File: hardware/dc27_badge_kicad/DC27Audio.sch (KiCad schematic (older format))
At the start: 21 parts, among them U501 CS4344-CZZ, U502 LM4880

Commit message: check in charging circuit changes
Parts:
- removed TP501: DAC_OUT_R, TestPoint:TestPoint_Pad_D2.0mm, symbol Connector:TestPoint
- removed TP502: DAC_OUT_L, TestPoint:TestPoint_Pad_D2.0mm, symbol Connector:TestPoint
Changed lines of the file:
@@
 	4250 3850 4500 3850
+Wire Wire Line
+	4550 4100 4700 4100
 Wire Wire Line
 	4550 3950 4550 4100
@@
 	5000 4100 5300 4100
 Wire Wire Line
-	4250 3650 4600 3650
+	4250 3650 4700 3650
 Wire Wire Line
 	5000 3650 5300 3650
@@
 Text Notes 4850 3350 0    50   ~ 0
 Can drop R502,503 to 15k, \nbut some distortion present.
-$Comp
-L Connector:TestPoint TP501
-U 1 1 5CE34BE7
-P 4600 3050
-F 0 "TP501" H 4658 3168 50  0000 L CNN
-F 1 "DAC_OUT_R" H 4658 3077 50  0000 L CNN
-F 2 "TestPoint:TestPoint_Pad_D2.0mm" H 4800 3050 50  0001 C CNN
-F 3 "~" H 4800 3050 50  0001 C CNN
-	1    4600 3050
-	1    0    0    -1
-$EndComp
-$Comp
-L Connector:TestPoint TP502
-U 1 1 5CE35CF0
-P 4600 4750
-F 0 "TP502" H 4542 4776 50  0000 R CNN
-F 1 "DAC_OUT_L" H 4542 4867 50  0000 R CNN
-F 2 "TestPoint:TestPoint_Pad_D2.0mm" H 4800 4750 50  0001 C CNN
-F 3 "~" H 4800 4750 50  0001 C CNN
-	1    4600 4750
-	-1   0    0    1
-$EndComp
-Wire Wire Line
-	4600 4750 4600 4100
-Wire Wire Line
-	4550 4100 4600 4100
-Connection ~ 4600 4100
-Wire Wire Line
-	4600 4100 4700 4100
-Wire Wire Line
-	4600 3050 4600 3650
-Connection ~ 4600 3650
-Wire Wire Line
-	4600 3650 4700 3650
 $EndSCHEMATC

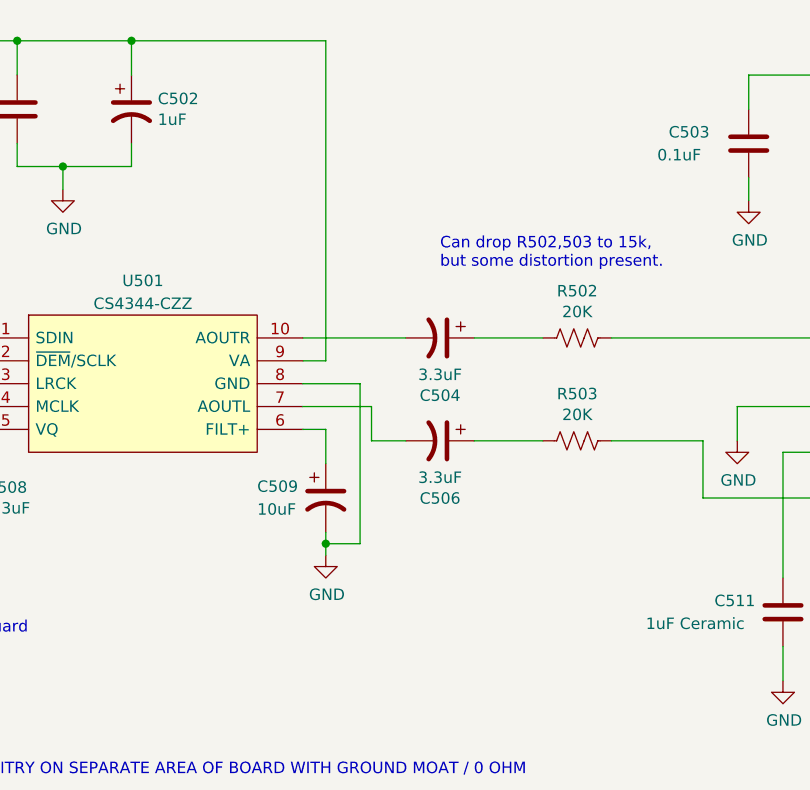
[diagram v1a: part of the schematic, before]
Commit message: add test points for DAC
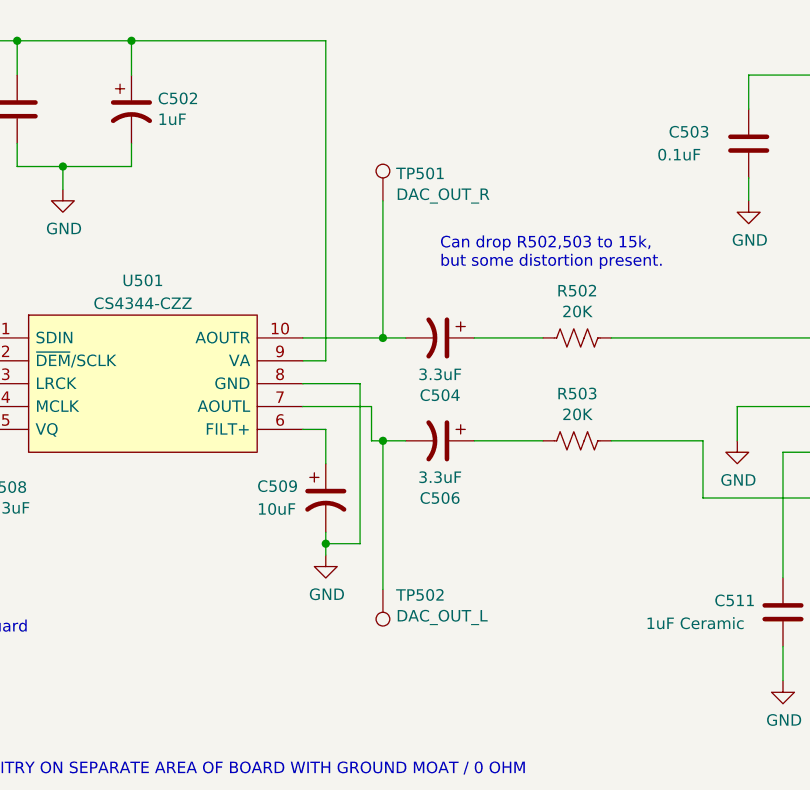
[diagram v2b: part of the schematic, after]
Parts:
- added TP501: DAC_OUT_R, TestPoint:TestPoint_Pad_D2.0mm, symbol Connector:TestPoint
- added TP502: DAC_OUT_L, TestPoint:TestPoint_Pad_D2.0mm, symbol Connector:TestPoint
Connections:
- net at C504.2, U501.10 (AOUTR): now also TP501.1
- net at C506.2, U501.7 (AOUTL): now also TP502.1
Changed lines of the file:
@@
 	4250 3850 4500 3850
-Wire Wire Line
-	4550 4100 4700 4100
 Wire Wire Line
 	4550 3950 4550 4100
@@
 	5000 4100 5300 4100
 Wire Wire Line
-	4250 3650 4700 3650
+	4250 3650 4600 3650
 Wire Wire Line
 	5000 3650 5300 3650
@@
 Text Notes 4850 3350 0    50   ~ 0
 Can drop R502,503 to 15k, \nbut some distortion present.
+$Comp
+L Connector:TestPoint TP501
+U 1 1 5CE34BE7
+P 4600 3050
+F 0 "TP501" H 4658 3168 50  0000 L CNN
+F 1 "DAC_OUT_R" H 4658 3077 50  0000 L CNN
+F 2 "TestPoint:TestPoint_Pad_D2.0mm" H 4800 3050 50  0001 C CNN
+F 3 "~" H 4800 3050 50  0001 C CNN
+	1    4600 3050
+	1    0    0    -1
+$EndComp
+$Comp
+L Connector:TestPoint TP502
+U 1 1 5CE35CF0
+P 4600 4750
+F 0 "TP502" H 4542 4776 50  0000 R CNN
+F 1 "DAC_OUT_L" H 4542 4867 50  0000 R CNN
+F 2 "TestPoint:TestPoint_Pad_D2.0mm" H 4800 4750 50  0001 C CNN
+F 3 "~" H 4800 4750 50  0001 C CNN
+	1    4600 4750
+	-1   0    0    1
+$EndComp
+Wire Wire Line
+	4600 4750 4600 4100
+Wire Wire Line
+	4550 4100 4600 4100
+Connection ~ 4600 4100
+Wire Wire Line
+	4600 4100 4700 4100
+Wire Wire Line
+	4600 3050 4600 3650
+Connection ~ 4600 3650
+Wire Wire Line
+	4600 3650 4700 3650
 $EndSCHEMATC
